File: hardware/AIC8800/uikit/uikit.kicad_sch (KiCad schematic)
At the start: 48 parts, among them J1 Conn_01x20, J2 Conn_01x20, J3 Conn_01x10, J4 Conn_01x06, J5 USB_C_Receptacle_USB2.0, J6 Micro_SD_Card_Det, J7 PJ-393-USA, U1 AIC1000A, U2 CH340N, U3 NS8002

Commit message: [hardware/aic8800/uikit] update
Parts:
- C11, C13: value 0.1uF -> 1.0uF
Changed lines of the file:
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@@
     (in_bom yes) (on_board yes)
     (property "Reference" "C11" (id 0) (at 79.375 129.54 90))
-    (property "Value" "0.1uF" (id 1) (at 78.74 132.08 90))
+    (property "Value" "1.0uF" (id 1) (at 78.74 132.08 90))
     (property "Footprint" "Capacitor_SMD:C_0402_1005Metric" (id 2) (at 86.36 129.8448 0)
       (effects (font (size 1.27 1.27)) hide)
@@
     (in_bom yes) (on_board yes)
     (property "Reference" "C13" (id 0) (at 69.215 142.24 90))
-    (property "Value" "0.1uF" (id 1) (at 68.58 139.065 90))
+    (property "Value" "1.0uF" (id 1) (at 68.58 139.065 90))
     (property "Footprint" "Capacitor_SMD:C_0402_1005Metric" (id 2) (at 76.2 140.0048 0)
       (effects (font (size 1.27 1.27)) hide)
@@
     )
     (path "/3625a949-0ec7-4992-8b3f-92ea9e8fc090"
-      (reference "C11") (unit 1) (value "0.1uF") (footprint "Capacitor_SMD:C_0402_1005Metric")
+      (reference "C11") (unit 1) (value "1.0uF") (footprint "Capacitor_SMD:C_0402_1005Metric")
     )
     (path "/090869a7-5d10-4fc0-b6da-f9a792cb3d45"
@@
     )
     (path "/d3b746a4-24d4-4d94-812d-8fdff5b5d7a6"
-      (reference "C13") (unit 1) (value "0.1uF") (footprint "Capacitor_SMD:C_0402_1005Metric")
+      (reference "C13") (unit 1) (value "1.0uF") (footprint "Capacitor_SMD:C_0402_1005Metric")
     )
     (path "/76a7f0ab-c33f-4240-89ef-a022300bf5dc"

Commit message: [hardware/aic8800m_uikit] add bootloader button
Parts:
- added SW0: SW_Push, VSF:Key_2Pin_2.9X4.3, symbol Switch:SW_Push
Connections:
- net B7: now also SW0.2
- net GND: now also SW0.1
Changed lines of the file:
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@@
+    (stroke (width 0) (type default) (color 0 0 0 0))
+  )
+  (wire (pts (xy 17.78 94.615) (xy 21.59 94.615))
     (stroke (width 0) (type default) (color 0 0 0 0))
   )
@@
   )
   (label "AU_XTAL" (at 48.26 130.175 180)
+    (effects (font (size 1.27 1.27)) (justify right bottom))
+  )
+  (label "GND" (at 21.59 94.615 180)
     (effects (font (size 1.27 1.27)) (justify right bottom))
   )
@@
     (pin "8")
     (pin "9")
+  )
+  (symbol (lib_id "Switch:SW_Push") (at 26.67 94.615 0) (unit 1)
+    (in_bom yes) (on_board yes) (fields_autoplaced)
+    (property "Reference" "SW0" (id 0) (at 26.67 87.9942 0))
+    (property "Value" "SW_Push" (id 1) (at 26.67 90.5311 0))
+    (property "Footprint" "VSF:Key_2Pin_2.9X4.3" (id 2) (at 26.67 89.535 0)
+      (effects (font (size 1.27 1.27)) hide)
+    )
+    (property "Datasheet" "~" (id 3) (at 26.67 89.535 0)
+      (effects (font (size 1.27 1.27)) hide)
+    )
+    (pin "1")
+    (pin "2")
   )
   (symbol (lib_id "power:GND") (at 180.975 51.435 90) (unit 1)
@@
       (reference "R23") (unit 1) (value "100K") (footprint "Resistor_SMD:R_0402_1005Metric")
     )
+    (path "/e2c38a64-8438-404e-87e4-3c9b4a23ac06"
+      (reference "SW0") (unit 1) (value "SW_Push") (footprint "VSF:Key_2Pin_2.9X4.3")
+    )
     (path "/ab0bba3b-9902-471a-8615-9dfda2c848da"

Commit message: [hardware/aic8800m/uikit] add GND pin
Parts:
- added J8: Conn_01x02, Connector_PinHeader_2.54mm:PinHeader_1x02_P2.54mm_Vertical, symbol Connector_Generic:Conn_01x02
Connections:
- net GND: now also J8.1 (Pin_1), J8.2 (Pin_2)
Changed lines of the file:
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@@
   (junction (at 103.505 24.765) (diameter 0) (color 0 0 0 0)
   )
+  (junction (at 43.18 152.4) (diameter 0) (color 0 0 0 0)
+  )
   (junction (at 137.795 137.16) (diameter 0) (color 0 0 0 0)
   )
@@
   )
   (wire (pts (xy 31.75 135.255) (xy 48.26 135.255))
+    (stroke (width 0) (type default) (color 0 0 0 0))
+  )
+  (wire (pts (xy 43.18 152.4) (xy 43.18 154.94))
     (stroke (width 0) (type default) (color 0 0 0 0))
   )
@@
   (symbol (lib_id "power:GND") (at 78.74 130.81 270) (unit 1)
     (in_bom yes) (on_board yes)
-    (property "Reference" "#PWR?" (id 0) (at 72.39 130.81 0)
+    (property "Reference" "#PWR0103" (id 0) (at 72.39 130.81 0)
       (effects (font (size 1.27 1.27)) hide)
     )
@@
   (symbol (lib_id "power:GND") (at 86.36 156.21 0) (unit 1)
     (in_bom yes) (on_board yes)
-    (property "Reference" "#PWR?" (id 0) (at 86.36 162.56 0)
+    (property "Reference" "#PWR0105" (id 0) (at 86.36 162.56 0)
       (effects (font (size 1.27 1.27)) hide)
     )
@@
     )
     (property "Datasheet" "" (id 3) (at 86.36 156.21 0)
+      (effects (font (size 1.27 1.27)) hide)
+    )
+    (pin "1")
+  )
+  (symbol (lib_id "power:GND") (at 43.18 152.4 270) (unit 1)
+    (in_bom yes) (on_board yes)
+    (property "Reference" "#PWR0106" (id 0) (at 36.83 152.4 0)
+      (effects (font (size 1.27 1.27)) hide)
+    )
+    (property "Value" "GND" (id 1) (at 40.005 153.035 0))
+    (property "Footprint" "" (id 2) (at 43.18 152.4 0)
+      (effects (font (size 1.27 1.27)) hide)
+    )
+    (property "Datasheet" "" (id 3) (at 43.18 152.4 0)
       (effects (font (size 1.27 1.27)) hide)
     )
@@
     (pin "1")
   )
+  (symbol (lib_id "Connector_Generic:Conn_01x02") (at 48.26 152.4 0) (unit 1)
+    (in_bom yes) (on_board yes) (fields_autoplaced)
+    (property "Reference" "J8" (id 0) (at 50.292 152.8353 0)
+      (effects (font (size 1.27 1.27)) (justify left))
+    )
+    (property "Value" "Conn_01x02" (id 1) (at 50.292 155.3722 0)
+      (effects (font (size 1.27 1.27)) (justify left))
+    )
+    (property "Footprint" "Connector_PinHeader_2.54mm:PinHeader_1x02_P2.54mm_Vertical" (id 2) (at 48.26 152.4 0)
+      (effects (font (size 1.27 1.27)) hide)
+    )
+    (property "Datasheet" "~" (id 3) (at 48.26 152.4 0)
+      (effects (font (size 1.27 1.27)) hide)
+    )
+    (pin "1")
+    (pin "2")
+  )
   (symbol (lib_id "Device:R") (at 141.605 121.92 270) (unit 1)
     (in_bom yes) (on_board yes)
@@
   (symbol (lib_id "power:GND") (at 68.58 140.97 270) (unit 1)
     (in_bom yes) (on_board yes)
-    (property "Reference" "#PWR?" (id 0) (at 62.23 140.97 0)
+    (property "Reference" "#PWR0104" (id 0) (at 62.23 140.97 0)
       (effects (font (size 1.27 1.27)) hide)
     )
@@
     )
     (path "/34d46911-498d-4734-b012-616470e77a13"
-      (reference "#PWR?") (unit 1) (value "GND") (footprint "")
+      (reference "#PWR0103") (unit 1) (value "GND") (footprint "")
+    )
+    (path "/86e82f02-f141-4176-acf6-4e6a12910c8d"
+      (reference "#PWR0104") (unit 1) (value "GND") (footprint "")
     )
     (path "/4f81cb89-d4f1-4511-9cfb-1c281e2a84ee"
-      (reference "#PWR?") (unit 1) (value "GND") (footprint "")
-    )
-    (path "/86e82f02-f141-4176-acf6-4e6a12910c8d"
-      (reference "#PWR?") (unit 1) (value "GND") (footprint "")
+      (reference "#PWR0105") (unit 1) (value "GND") (footprint "")
+    )
+    (path "/52bd9912-060d-4e00-8fd0-391130c9d460"
+      (reference "#PWR0106") (unit 1) (value "GND") (footprint "")
     )
     (path "/faf7f873-d004-44e5-b2bd-9d7562f28cb5"
@@
       (reference "J7") (unit 1) (value "PJ-393-USA") (footprint "VSF:PJ-393")
     )
+    (path "/74435c32-41e2-4190-a0c3-bfb62d12c674"
+      (reference "J8") (unit 1) (value "Conn_01x02") (footprint "Connector_PinHeader_2.54mm:PinHeader_1x02_P2.54mm_Vertical")
+    )
     (path "/b9d2e5e4-c0aa-4123-bebf-50231b0e2b27"

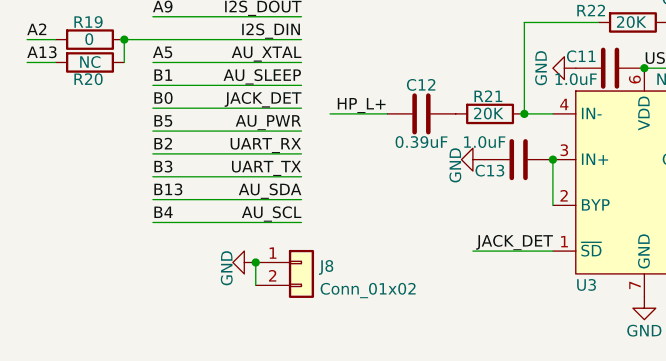
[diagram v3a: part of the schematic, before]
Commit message: [hardware/aic8800m/uikit] add pin for debug uart
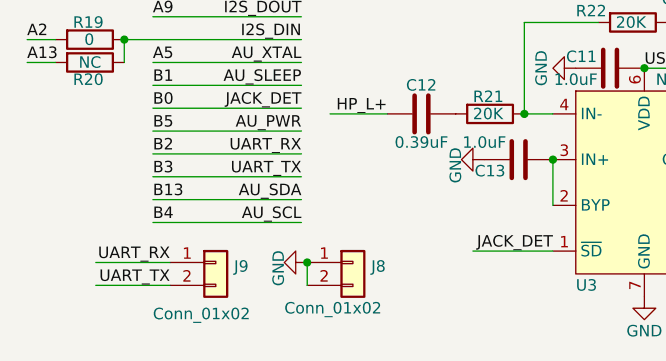
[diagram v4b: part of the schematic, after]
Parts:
- added J9: Conn_01x02, Connector_PinHeader_2.54mm:PinHeader_1x02_P2.54mm_Vertical, symbol Connector_Generic:Conn_01x02
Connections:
- net B2: now also J9.1 (Pin_1)
- net B3: now also J9.2 (Pin_2)
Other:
- moved on the sheet: J8
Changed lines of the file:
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@@
   (junction (at 103.505 24.765) (diameter 0) (color 0 0 0 0)
   )
-  (junction (at 43.18 152.4) (diameter 0) (color 0 0 0 0)
+  (junction (at 48.895 152.4) (diameter 0) (color 0 0 0 0)
   )
   (junction (at 137.795 137.16) (diameter 0) (color 0 0 0 0)
@@
     (stroke (width 0) (type default) (color 0 0 0 0))
   )
+  (wire (pts (xy 25.4 152.4) (xy 33.655 152.4))
+    (stroke (width 0) (type default) (color 0 0 0 0))
+  )
   (wire (pts (xy 98.425 28.575) (xy 98.425 24.765))
     (stroke (width 0) (type default) (color 0 0 0 0))
@@
     (stroke (width 0) (type default) (color 0 0 0 0))
   )
+  (wire (pts (xy 25.4 154.94) (xy 33.655 154.94))
+    (stroke (width 0) (type default) (color 0 0 0 0))
+  )
   (wire (pts (xy 31.75 86.995) (xy 48.26 86.995))
     (stroke (width 0) (type default) (color 0 0 0 0))
@@
     (stroke (width 0) (type default) (color 0 0 0 0))
   )
-  (wire (pts (xy 43.18 152.4) (xy 43.18 154.94))
+  (wire (pts (xy 48.895 152.4) (xy 48.895 154.94))
     (stroke (width 0) (type default) (color 0 0 0 0))
   )
@@
     (effects (font (size 1.27 1.27)) (justify right bottom))
   )
+  (label "UART_TX" (at 33.655 154.94 180)
+    (effects (font (size 1.27 1.27)) (justify right bottom))
+  )
   (label "A1" (at 17.78 117.475 0)
     (effects (font (size 1.27 1.27)) (justify left bottom))
@@
   (label "B7" (at 31.75 92.075 0)
     (effects (font (size 1.27 1.27)) (justify left bottom))
+  )
+  (label "UART_RX" (at 33.655 152.4 180)
+    (effects (font (size 1.27 1.27)) (justify right bottom))
   )
   (label "A1" (at 48.26 31.75 180)
@@
     (pin "1")
   )
-  (symbol (lib_id "power:GND") (at 43.18 152.4 270) (unit 1)
-    (in_bom yes) (on_board yes)
-    (property "Reference" "#PWR0106" (id 0) (at 36.83 152.4 0)
-      (effects (font (size 1.27 1.27)) hide)
-    )
-    (property "Value" "GND" (id 1) (at 40.005 153.035 0))
-    (property "Footprint" "" (id 2) (at 43.18 152.4 0)
-      (effects (font (size 1.27 1.27)) hide)
-    )
-    (property "Datasheet" "" (id 3) (at 43.18 152.4 0)
+  (symbol (lib_id "power:GND") (at 48.895 152.4 270) (unit 1)
+    (in_bom yes) (on_board yes)
+    (property "Reference" "#PWR0106" (id 0) (at 42.545 152.4 0)
+      (effects (font (size 1.27 1.27)) hide)
+    )
+    (property "Value" "GND" (id 1) (at 45.72 153.035 0))
+    (property "Footprint" "" (id 2) (at 48.895 152.4 0)
+      (effects (font (size 1.27 1.27)) hide)
+    )
+    (property "Datasheet" "" (id 3) (at 48.895 152.4 0)
       (effects (font (size 1.27 1.27)) hide)
     )
@@
     (pin "1")
   )
-  (symbol (lib_id "Connector_Generic:Conn_01x02") (at 48.26 152.4 0) (unit 1)
-    (in_bom yes) (on_board yes) (fields_autoplaced)
-    (property "Reference" "J8" (id 0) (at 50.292 152.8353 0)
-      (effects (font (size 1.27 1.27)) (justify left))
-    )
-    (property "Value" "Conn_01x02" (id 1) (at 50.292 155.3722 0)
-      (effects (font (size 1.27 1.27)) (justify left))
-    )
-    (property "Footprint" "Connector_PinHeader_2.54mm:PinHeader_1x02_P2.54mm_Vertical" (id 2) (at 48.26 152.4 0)
-      (effects (font (size 1.27 1.27)) hide)
-    )
-    (property "Datasheet" "~" (id 3) (at 48.26 152.4 0)
+  (symbol (lib_id "Connector_Generic:Conn_01x02") (at 53.975 152.4 0) (unit 1)
+    (in_bom yes) (on_board yes)
+    (property "Reference" "J8" (id 0) (at 56.007 152.8353 0)
+      (effects (font (size 1.27 1.27)) (justify left))
+    )
+    (property "Value" "Conn_01x02" (id 1) (at 46.355 157.48 0)
+      (effects (font (size 1.27 1.27)) (justify left))
+    )
+    (property "Footprint" "Connector_PinHeader_2.54mm:PinHeader_1x02_P2.54mm_Vertical" (id 2) (at 53.975 152.4 0)
+      (effects (font (size 1.27 1.27)) hide)
+    )
+    (property "Datasheet" "~" (id 3) (at 53.975 152.4 0)
       (effects (font (size 1.27 1.27)) hide)
     )
@@
     )
     (property "Datasheet" "~" (id 3) (at 121.92 86.36 0)
+      (effects (font (size 1.27 1.27)) hide)
+    )
+    (pin "1")
+    (pin "2")
+  )
+  (symbol (lib_id "Connector_Generic:Conn_01x02") (at 38.735 152.4 0) (unit 1)
+    (in_bom yes) (on_board yes)
+    (property "Reference" "J9" (id 0) (at 40.767 152.8353 0)
+      (effects (font (size 1.27 1.27)) (justify left))
+    )
+    (property "Value" "Conn_01x02" (id 1) (at 31.75 158.115 0)
+      (effects (font (size 1.27 1.27)) (justify left))
+    )
+    (property "Footprint" "Connector_PinHeader_2.54mm:PinHeader_1x02_P2.54mm_Vertical" (id 2) (at 38.735 152.4 0)
+      (effects (font (size 1.27 1.27)) hide)
+    )
+    (property "Datasheet" "~" (id 3) (at 38.735 152.4 0)
       (effects (font (size 1.27 1.27)) hide)
     )
@@
       (reference "J8") (unit 1) (value "Conn_01x02") (footprint "Connector_PinHeader_2.54mm:PinHeader_1x02_P2.54mm_Vertical")
     )
+    (path "/a919e9a2-2f6f-4889-8b57-eda01e4271ad"
+      (reference "J9") (unit 1) (value "Conn_01x02") (footprint "Connector_PinHeader_2.54mm:PinHeader_1x02_P2.54mm_Vertical")
+    )
     (path "/b9d2e5e4-c0aa-4123-bebf-50231b0e2b27"
